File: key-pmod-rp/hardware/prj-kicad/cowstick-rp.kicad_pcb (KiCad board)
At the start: 2 copper layers, 45 x 19 mm, 3 parts, among them J2 PMOD, P1 CONN_USB-A, U1 RP2040

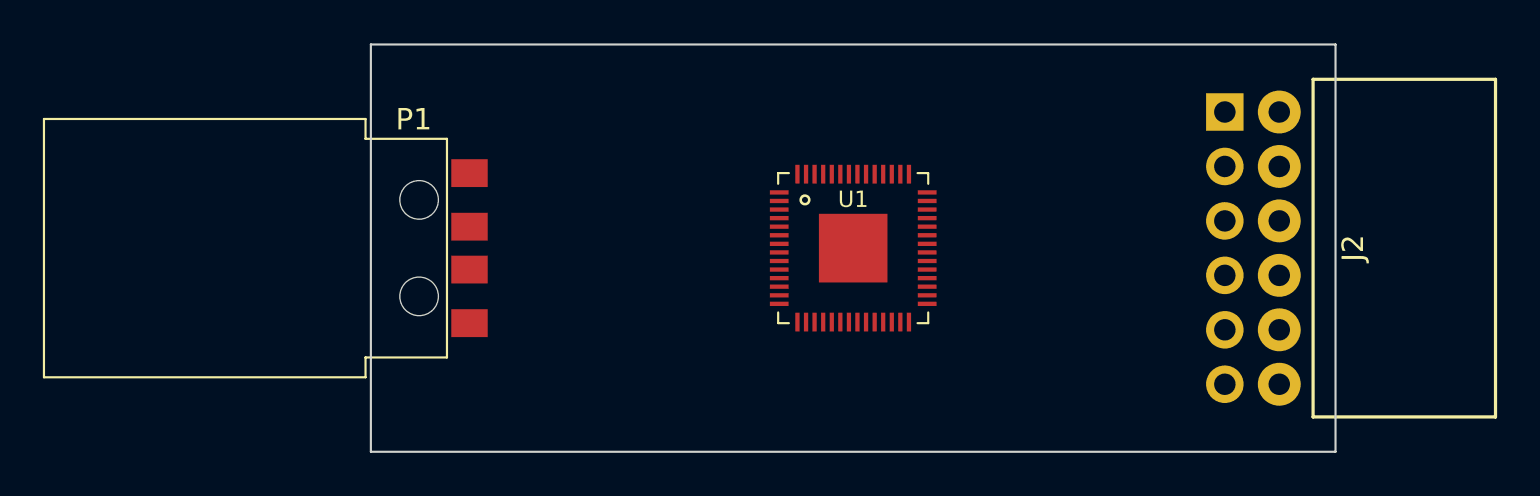
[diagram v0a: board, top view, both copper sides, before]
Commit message: KeyPMOD: Improve PCB r1, add power supply (5V->3V3)
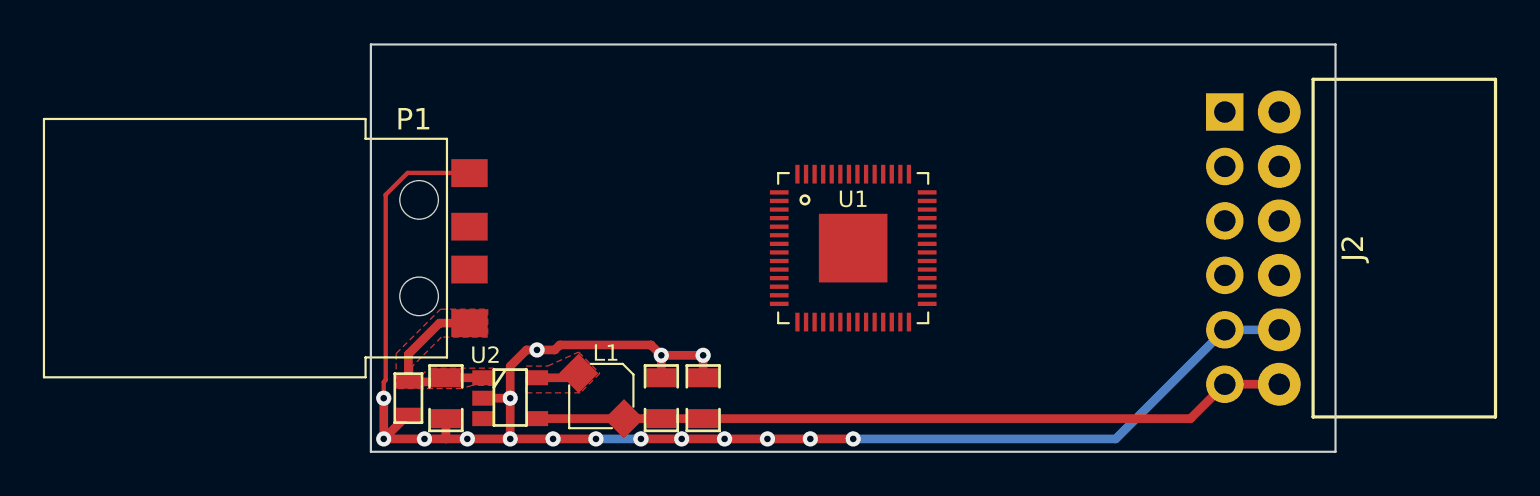
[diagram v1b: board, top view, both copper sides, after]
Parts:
- added C1: 10uF, cowstick-rp:SMD0805, F.Cu at (129.5, 112.0)
- added C2: 470pF, cowstick-rp:SMD0603, F.Cu at (127.8, 112.0)
- added C3: 4,7uF, cowstick-rp:SMD0805, F.Cu at (139.6, 112.0)
- added C4: 4,7uF, cowstick-rp:SMD0805, F.Cu at (141.5, 112.0)
- added L1: 2,2uH, cowstick-rp:I_CDRH2D14, F.Cu at (136.8, 111.9)
- added U2: LM3671, cowstick-rp:SOT23-5, F.Cu at (132.5, 112.0)
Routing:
- net GND: track 0.00 -> 78.6 mm, vias 0 -> 17
- net +3.3V: track 0.00 -> 35.3 mm
- net +VBus: track 0.00 -> 8.30 mm
- net Net-(L1-Pad1): track 0.00 -> 2.01 mm
- added copper zone on F.Cu, net +VBus
- added copper zone on F.Cu, net Net-(L1-Pad1)

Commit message: KeyPMOD: Improve PCB r1, add RP2040 mcu (include crystal and decoupling caps)
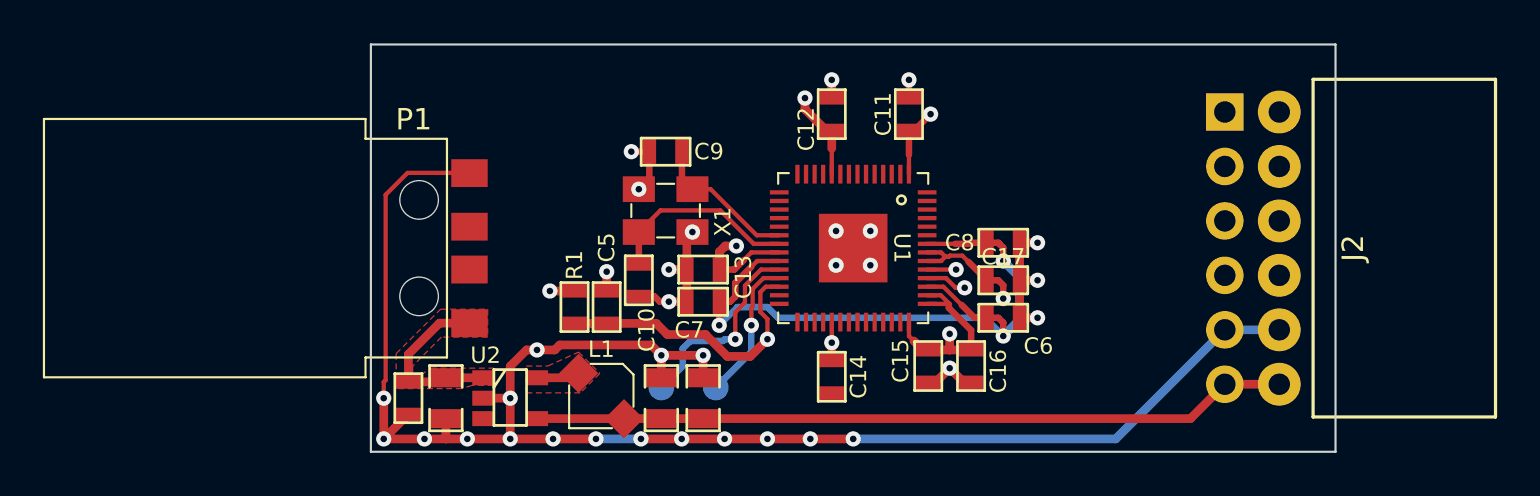
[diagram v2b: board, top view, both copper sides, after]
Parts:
- added C10: 10pF, cowstick-rp:SMD0603, F.Cu at (138.5, 106.5)
- added C11: 100nF, cowstick-rp:SMD0603, F.Cu at (151.1, 98.8)
- added C12: 100nF, cowstick-rp:SMD0603, F.Cu at (147.5, 98.8)
- added C13: 100nF, cowstick-rp:SMD0603, F.Cu at (141.5, 106.0)
- added C14: 100nF, cowstick-rp:SMD0603, F.Cu at (147.5, 111.0)
- added C15: 100nF, cowstick-rp:SMD0603, F.Cu at (152.0, 110.5)
- added C16: 100nF, cowstick-rp:SMD0603, F.Cu at (154.0, 110.5)
- added C17: 100nF, cowstick-rp:SMD0603, F.Cu at (155.5, 106.5)
- added C5: 1uF, cowstick-rp:SMD0603, F.Cu at (137.0, 107.8)
- added C6: 1uF, cowstick-rp:SMD0603, F.Cu at (155.5, 108.2)
- added C7: 100nF, cowstick-rp:SMD0603, F.Cu at (141.5, 107.5)
- added C8: 100nF, cowstick-rp:SMD0603, F.Cu at (155.5, 104.8)
- added C9: 10pF, cowstick-rp:SMD0603, F.Cu at (139.8, 100.5)
- added R1: 10k, cowstick-rp:SMD0603, F.Cu at (135.5, 107.8)
- added TP4: CONN_1, cowstick-rp:TP_SMD, B.Cu at (139.6, 111.5)
- added TP5: CONN_1, cowstick-rp:TP_SMD, B.Cu at (142.1, 111.5)
- added X1: 12MHz, cowstick-rp:Q_3.2x2.5, F.Cu at (139.8, 103.2)
- turned U1 to -90 degrees
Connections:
- U1 pad 1: unconnected-(U1-Pad1) -> +3.3V
- U1 pad 10: unconnected-(U1-Pad10) -> +3.3V
- U1 pad 20: unconnected-(U1-Pad20) -> Net-(C9-Pad1)
- U1 pad 21: unconnected-(U1-Pad21) -> Net-(C10-Pad1)
- U1 pad 22: unconnected-(U1-Pad22) -> +3.3V
- U1 pad 23: unconnected-(U1-Pad23) -> Net-(C6-Pad1)
- U1 pad 24: unconnected-(U1-Pad24) -> Net-(TP4-Pad1)
- U1 pad 25: unconnected-(U1-Pad25) -> Net-(TP5-Pad1)
- U1 pad 26: unconnected-(U1-Pad26) -> RST
- U1 pad 33: unconnected-(U1-Pad33) -> +3.3V
- U1 pad 42: unconnected-(U1-Pad42) -> +3.3V
- U1 pad 43: unconnected-(U1-Pad43) -> +3.3V
- U1 pad 44: unconnected-(U1-Pad44) -> +3.3V
- U1 pad 45: unconnected-(U1-Pad45) -> Net-(C6-Pad1)
- U1 pad 48: unconnected-(U1-Pad48) -> +3.3V
- U1 pad 49: unconnected-(U1-Pad49) -> +3.3V
- U1 pad 50: unconnected-(U1-Pad50) -> Net-(C6-Pad1)
- U1 pad PAD: unconnected-(U1-PadPAD) -> GND
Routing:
- net Net-(C6-Pad1): track 0.00 -> 32.5 mm, vias 0 -> 3
- net +3.3V: track 35.3 -> 65.8 mm, vias 0 -> 7
- net GND: track 78.6 -> 99.0 mm, vias 17 -> 33
- net RST: track 0.00 -> 13.3 mm, vias 0 -> 1
- net Net-(TP4-Pad1): track 0.00 -> 9.45 mm, vias 0 -> 1
- net Net-(C10-Pad1): track 0.00 -> 9.10 mm
- net Net-(C9-Pad1): track 0.00 -> 6.89 mm
- net Net-(TP5-Pad1): track 0.00 -> 6.76 mm, vias 0 -> 1
- net unconnected-(U1-Pad46): track 0.00 -> 1.94 mm, vias 0 -> 1
- net unconnected-(U1-Pad47): track 0.00 -> 1.35 mm, vias 0 -> 1

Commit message: KeyPMOD: Add flash memory and USB protection. Design of board rev1 mostly finish
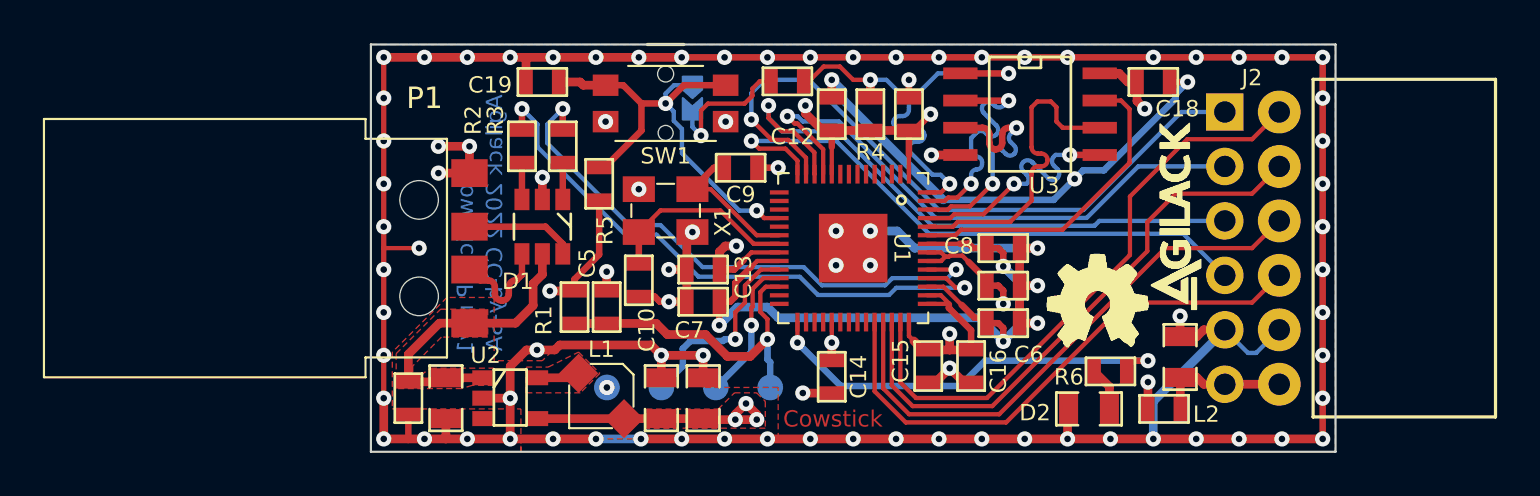
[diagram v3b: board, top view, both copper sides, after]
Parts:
- added C18: 100nF, cowstick-rp:SMD0603, F.Cu at (162.5, 97.2)
- added C19: 100nF, cowstick-rp:SMD0603, F.Cu at (134.0, 97.2)
- added C20: 10uF, cowstick-rp:SMD0805, F.Cu at (163.8, 110.1)
- added D1: USBLC6-2, cowstick-rp:SOT23-6, F.Cu at (134.0, 104.0)
- added D2: LED, cowstick-rp:SMD0805, F.Cu at (159.5, 112.5)
- added JP1: JUMPER, cowstick-rp:TP_JP, B.Cu at (141.0, 98.0)
- added L2: FB100, cowstick-rp:SMD0603, F.Cu at (163.0, 112.5)
- added R2: 23, cowstick-rp:SMD0603, F.Cu at (133.1, 100.2)
- added R3: 23, cowstick-rp:SMD0603, F.Cu at (134.9, 100.2)
- added R4: 10k, cowstick-rp:SMD0603, F.Cu at (149.3, 98.8)
- added R5: 10k, cowstick-rp:SMD0603, F.Cu at (136.7, 102.0)
- added R6: 470, cowstick-rp:SMD0603, F.Cu at (160.5, 110.8)
- added R7: 1k, cowstick-rp:SMD0603, F.Cu at (145.4, 97.2)
- added SW1: SW_PUSH, cowstick-rp:SW_436351045816, F.Cu at (139.8, 98.2)
- added TP1: CONN_1, cowstick-rp:TP_SMD, B.Cu at (137.0, 111.5)
- added TP3: CONN_1, cowstick-rp:TP_SMD, B.Cu at (144.6, 111.5)
- added U3: W25Q16JV, cowstick-rp:SOIC-8, F.Cu at (156.8, 98.8)
- added agilack-11.5: 450px, cowstick-rp:logo-agilack, F.Cu at (163.5, 104.5)
- added ohw_logo: VAL**, cowstick-rp:logo-ohw, F.Cu at (159.9, 107.6)
- moved C9 3.58 mm to (143.2, 101.2), turned to 0 degrees
- moved C17 0.25 mm to (155.5, 106.8)
- moved C6 0.25 mm to (155.5, 108.5)
- moved C8 0.25 mm to (155.5, 105.0)
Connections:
- J2 pad 1: unconnected-(J2-Pad1) -> PMOD_CTS
- J2 pad 10: unconnected-(J2-Pad10) -> PMOD_IO8
- J2 pad 12: +3.3V -> +PMOD
- J2 pad 2: unconnected-(J2-Pad2) -> PMOD_TX
- J2 pad 3: unconnected-(J2-Pad3) -> PMOD_RX
- J2 pad 4: unconnected-(J2-Pad4) -> PMOD_RTS
- J2 pad 6: +3.3V -> +PMOD
- J2 pad 7: unconnected-(J2-Pad7) -> PMOD_IO5
- J2 pad 8: unconnected-(J2-Pad8) -> PMOD_IO6
- J2 pad 9: unconnected-(J2-Pad9) -> PMOD_IO7
- P1 pad 2: unconnected-(P1-Pad2) -> Net-(D1-Pad4)
- P1 pad 3: unconnected-(P1-Pad3) -> Net-(D1-Pad6)
- U1 pad 11: unconnected-(U1-Pad11) -> PMOD_TX
- U1 pad 12: unconnected-(U1-Pad12) -> PMOD_RX
- U1 pad 13: unconnected-(U1-Pad13) -> PMOD_CTS
- U1 pad 14: unconnected-(U1-Pad14) -> PMOD_RTS
- U1 pad 18: unconnected-(U1-Pad18) -> BUTTON
- U1 pad 29: unconnected-(U1-Pad29) -> LED
- U1 pad 38: unconnected-(U1-Pad38) -> PMOD_IO8
- U1 pad 39: unconnected-(U1-Pad39) -> PMOD_IO7
- U1 pad 40: unconnected-(U1-Pad40) -> PMOD_IO6
- U1 pad 41: unconnected-(U1-Pad41) -> PMOD_IO5
- U1 pad 46: unconnected-(U1-Pad46) -> USB_D-
- U1 pad 47: unconnected-(U1-Pad47) -> USB_D+
- U1 pad 51: unconnected-(U1-Pad51) -> FL_D3
- U1 pad 52: unconnected-(U1-Pad52) -> /FL_SCK
- U1 pad 53: unconnected-(U1-Pad53) -> FL_D0
- U1 pad 54: unconnected-(U1-Pad54) -> FL_D2
- U1 pad 55: unconnected-(U1-Pad55) -> FL_D1
- U1 pad 56: unconnected-(U1-Pad56) -> UB
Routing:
- net GND: track 99.0 -> 326.4 mm, vias 33 -> 94
- net +3.3V: track 65.8 -> 137.3 mm, vias 7 -> 12
- net PMOD_CTS: track 0.00 -> 32.0 mm, vias 0 -> 1
- net PMOD_RX: track 0.00 -> 28.4 mm, vias 0 -> 1
- net USB_D-: track 0.00 -> 27.9 mm, vias 0 -> 2
- net PMOD_IO5: track 0.00 -> 27.9 mm
- net PMOD_RTS: track 0.00 -> 27.8 mm, vias 0 -> 1
- net PMOD_IO6: track 0.00 -> 26.9 mm
- net PMOD_TX: track 0.00 -> 26.8 mm, vias 0 -> 1
- net USB_D+: track 0.00 -> 26.4 mm, vias 0 -> 2
- net PMOD_IO7: track 0.00 -> 25.8 mm
- net PMOD_IO8: track 0.00 -> 25.5 mm
- net BUTTON: track 0.00 -> 22.8 mm, vias 0 -> 2
- net UB: track 0.00 -> 22.3 mm, vias 0 -> 3
- net LED: track 0.00 -> 19.9 mm, vias 0 -> 2
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- added copper zone on F.Cu, net +3.3V
- added copper zone on In2.Cu, net +3.3V
- added copper zone on B.Cu, net GND
- added copper zone on F.Cu, net GND
- added copper zone on In1.Cu, net GND
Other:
- copper layers 2 -> 4
- board text added: "Agilack 2022 CC-by-SA"
- board text added: "Cowstick"
- board text added: "CowstickRP rev1"
